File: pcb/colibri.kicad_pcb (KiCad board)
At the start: 2 copper layers, 55 parts

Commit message: diodes on place
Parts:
- ld-1, ld-10, ld-11, ld-12, ld-13, ld-14, ld-15, ld-16, ld-17, ld-18, ld-19, ld-2, ld-20, ld-21, ld-22, ld-23, ld-24, ld-25, ld-26, ld-27, ld-3, ld-4, ld-5, ld-6, ld-7, ld-8, ld-9: footprint kbd:D3_TH_SMD_v2 -> kbd:D3_SMD_v2; moved to B.Cu
- pro-micro1: moved to B.Cu
- moved ld-5 124.9 mm to (201.1, 52.0), turned to 90 degrees
- moved ld-10 114.8 mm to (182.0, 71.1), turned to 90 degrees
- moved ld-13 112.8 mm to (122.6, 90.1), turned to 90 degrees
- moved ld-3 111.8 mm to (163.0, 52.0), turned to 90 degrees
- moved ld-12 107.1 mm to (220.1, 71.1), turned to 90 degrees
- moved ld-27 104.9 mm to (222.1, 128.2), turned to 90 degrees
- moved ld-1 100.9 mm to (122.6, 52.0), turned to 90 degrees
- moved ld-23 92.9 mm to (201.1, 109.2), turned to 90 degrees
- moved ld-6 90.7 mm to (220.1, 52.0), turned to 90 degrees
- moved ld-8 90.4 mm to (143.9, 71.1), turned to 90 degrees
- moved ld-11 88.3 mm to (201.1, 71.1), turned to 90 degrees
- moved ld-7 84.3 mm to (122.6, 71.1), turned to 90 degrees
- moved ld-17 82.8 mm to (201.1, 90.1), turned to 90 degrees
- moved ld-26 77.7 mm to (194.1, 128.2), turned to 90 degrees
- moved ld-21 77.2 mm to (163.0, 109.2), turned to 90 degrees
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
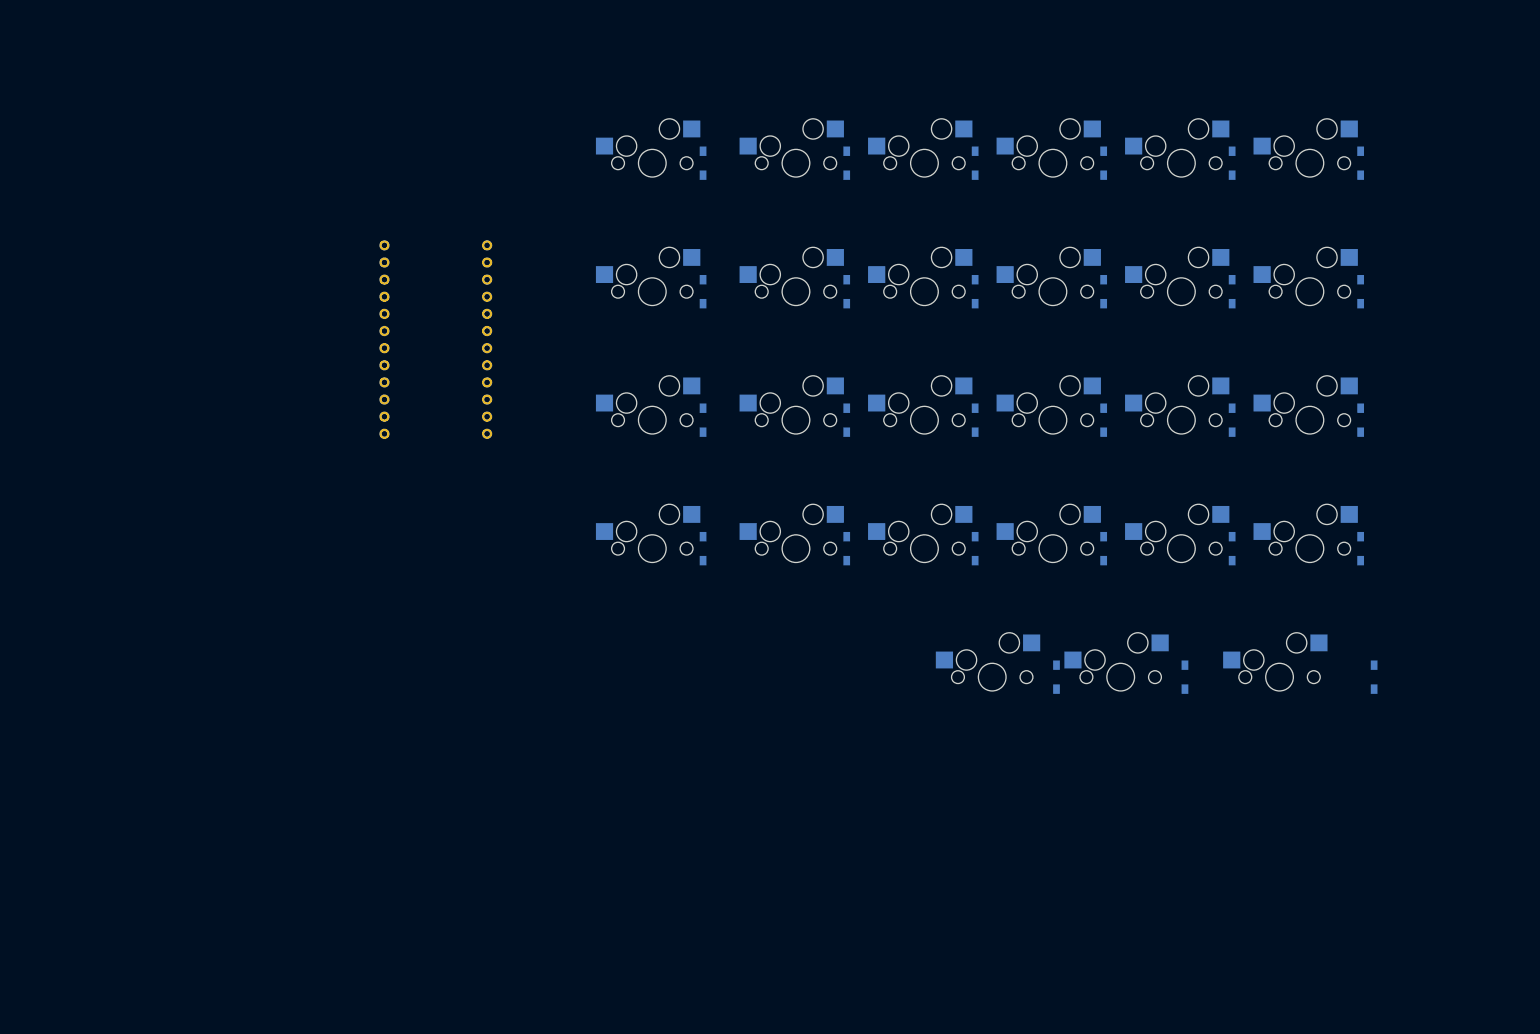
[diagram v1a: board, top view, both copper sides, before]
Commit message: LEDs placed on the PCB
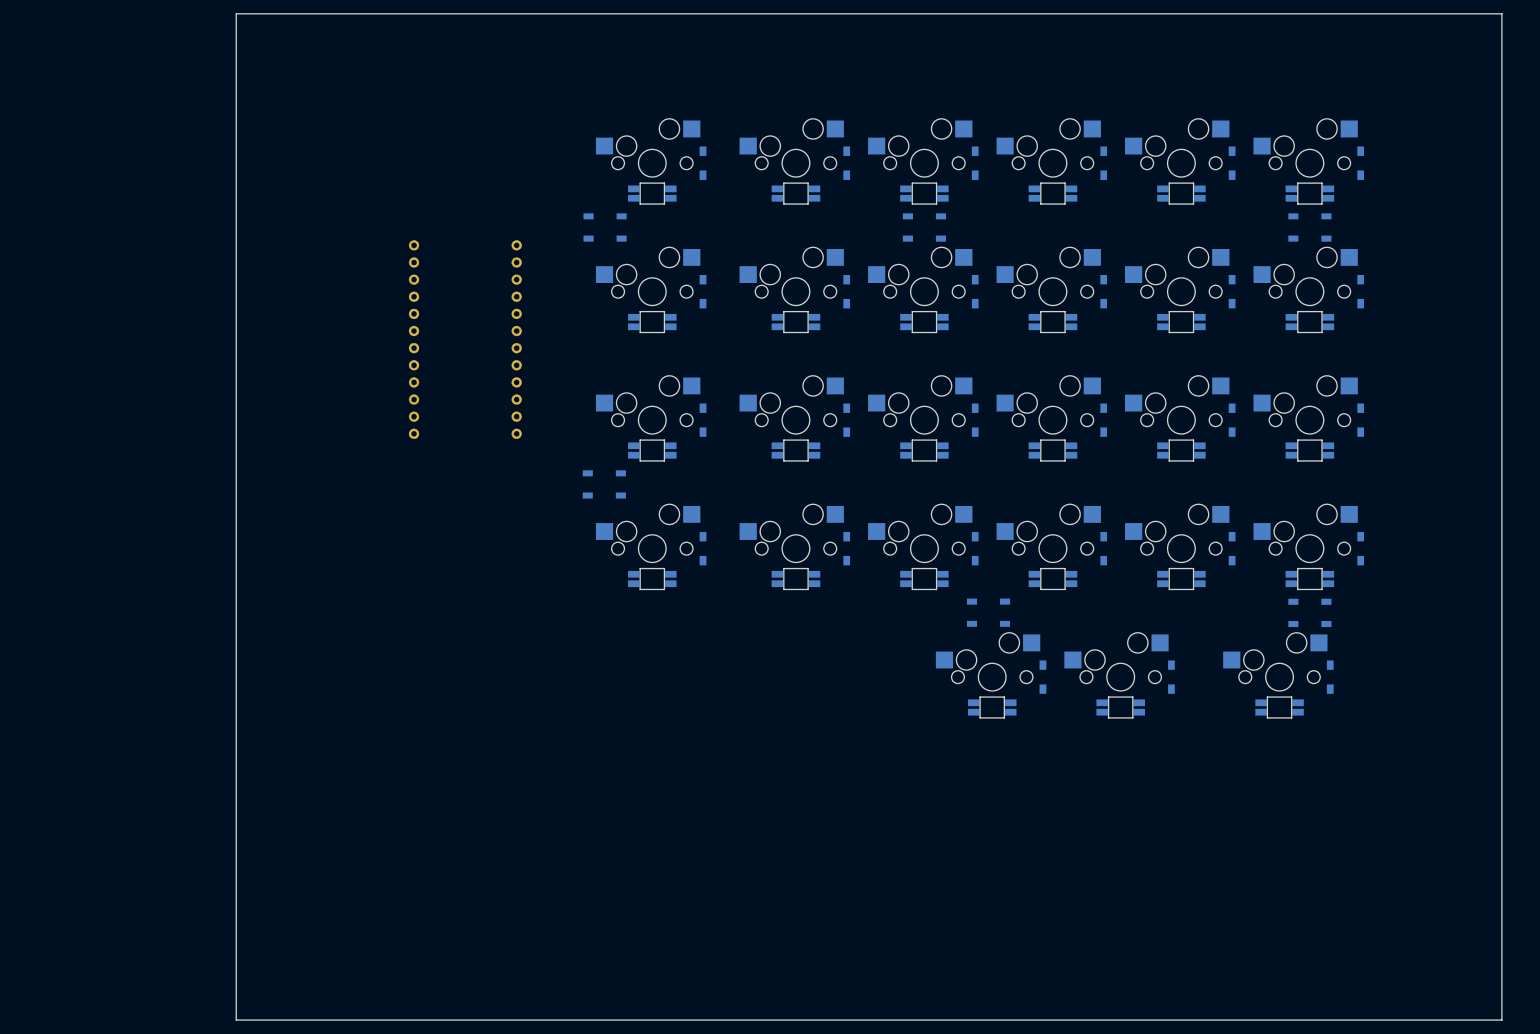
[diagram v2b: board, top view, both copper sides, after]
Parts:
- added lled-1: YS-SK6812MINI-E, kbd:YS-SK6812MINI-E, B.Cu at (115.1, 56.5)
- added lled-10: YS-SK6812MINI-E, kbd:YS-SK6812MINI-E, B.Cu at (174.5, 75.6)
- added lled-11: YS-SK6812MINI-E, kbd:YS-SK6812MINI-E, B.Cu at (193.6, 75.6)
- added lled-12: YS-SK6812MINI-E, kbd:YS-SK6812MINI-E, B.Cu at (212.6, 75.6)
- added lled-13: YS-SK6812MINI-E, kbd:YS-SK6812MINI-E, B.Cu at (115.1, 94.6)
- added lled-14: YS-SK6812MINI-E, kbd:YS-SK6812MINI-E, B.Cu at (136.4, 94.6)
- added lled-15: YS-SK6812MINI-E, kbd:YS-SK6812MINI-E, B.Cu at (155.5, 94.6)
- added lled-16: YS-SK6812MINI-E, kbd:YS-SK6812MINI-E, B.Cu at (174.5, 94.6)
- added lled-17: YS-SK6812MINI-E, kbd:YS-SK6812MINI-E, B.Cu at (193.6, 94.6)
- added lled-18: YS-SK6812MINI-E, kbd:YS-SK6812MINI-E, B.Cu at (212.6, 94.6)
- added lled-19: YS-SK6812MINI-E, kbd:YS-SK6812MINI-E, B.Cu at (115.1, 113.7)
- added lled-2: YS-SK6812MINI-E, kbd:YS-SK6812MINI-E, B.Cu at (136.4, 56.5)
- added lled-20: YS-SK6812MINI-E, kbd:YS-SK6812MINI-E, B.Cu at (136.4, 113.7)
- added lled-21: YS-SK6812MINI-E, kbd:YS-SK6812MINI-E, B.Cu at (155.5, 113.7)
- added lled-22: YS-SK6812MINI-E, kbd:YS-SK6812MINI-E, B.Cu at (174.5, 113.7)
- added lled-23: YS-SK6812MINI-E, kbd:YS-SK6812MINI-E, B.Cu at (193.6, 113.7)
- added lled-24: YS-SK6812MINI-E, kbd:YS-SK6812MINI-E, B.Cu at (212.6, 113.7)
- added lled-25: YS-SK6812MINI-E, kbd:YS-SK6812MINI-E, B.Cu at (165.5, 132.7)
- added lled-26: YS-SK6812MINI-E, kbd:YS-SK6812MINI-E, B.Cu at (184.6, 132.7)
- added lled-27: YS-SK6812MINI-E, kbd:YS-SK6812MINI-E, B.Cu at (208.1, 132.7)
- added lled-3: YS-SK6812MINI-E, kbd:YS-SK6812MINI-E, B.Cu at (155.5, 56.5)
- added lled-4: YS-SK6812MINI-E, kbd:YS-SK6812MINI-E, B.Cu at (174.5, 56.5)
- added lled-5: YS-SK6812MINI-E, kbd:YS-SK6812MINI-E, B.Cu at (193.6, 56.5)
- added lled-6: YS-SK6812MINI-E, kbd:YS-SK6812MINI-E, B.Cu at (212.6, 56.5)
- added lled-7: YS-SK6812MINI-E, kbd:YS-SK6812MINI-E, B.Cu at (115.1, 75.6)
- added lled-8: YS-SK6812MINI-E, kbd:YS-SK6812MINI-E, B.Cu at (136.4, 75.6)
- added lled-9: YS-SK6812MINI-E, kbd:YS-SK6812MINI-E, B.Cu at (155.5, 75.6)
- added lu-1: WS2812B, LED_SMD:LED_WS2812B_PLCC4_5.0x5.0mm_P3.2mm, B.Cu at (108.1, 61.6)
- added lu-2: WS2812B, LED_SMD:LED_WS2812B_PLCC4_5.0x5.0mm_P3.2mm, B.Cu at (155.5, 61.6)
- added lu-3: WS2812B, LED_SMD:LED_WS2812B_PLCC4_5.0x5.0mm_P3.2mm, B.Cu at (212.6, 61.6)
- added lu-4: WS2812B, LED_SMD:LED_WS2812B_PLCC4_5.0x5.0mm_P3.2mm, B.Cu at (108.0, 99.7)
- added lu-5: WS2812B, LED_SMD:LED_WS2812B_PLCC4_5.0x5.0mm_P3.2mm, B.Cu at (165.0, 118.7)
- added lu-6: WS2812B, LED_SMD:LED_WS2812B_PLCC4_5.0x5.0mm_P3.2mm, B.Cu at (212.6, 118.7)
- moved ld-27 6.50 mm to (215.6, 128.2)
- moved pro-micro1 4.39 mm to (87.4, 78.7)
- moved ld-25 2.00 mm to (173.0, 128.2)
- moved ld-26 2.00 mm to (192.1, 128.2)
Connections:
- pro-micro1 pad 1: unconnected-(pro-micro1-Pad1) -> lled
- pro-micro1 pad 2: unconnected-(pro-micro1-Pad2) -> ldata
- pro-micro1 pad 21: unconnected-(pro-micro1-Pad21) -> lVCC
- pro-micro1 pad 22: unconnected-(pro-micro1-Pad22) -> lreset
- pro-micro1 pad 23: unconnected-(pro-micro1-Pad23) -> lGND
- pro-micro1 pad 3: unconnected-(pro-micro1-Pad3) -> lGND
- pro-micro1 pad 4: unconnected-(pro-micro1-Pad4) -> lGND
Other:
- board outline added: 187.7 x 149.2 mm

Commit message: better keyboard layout
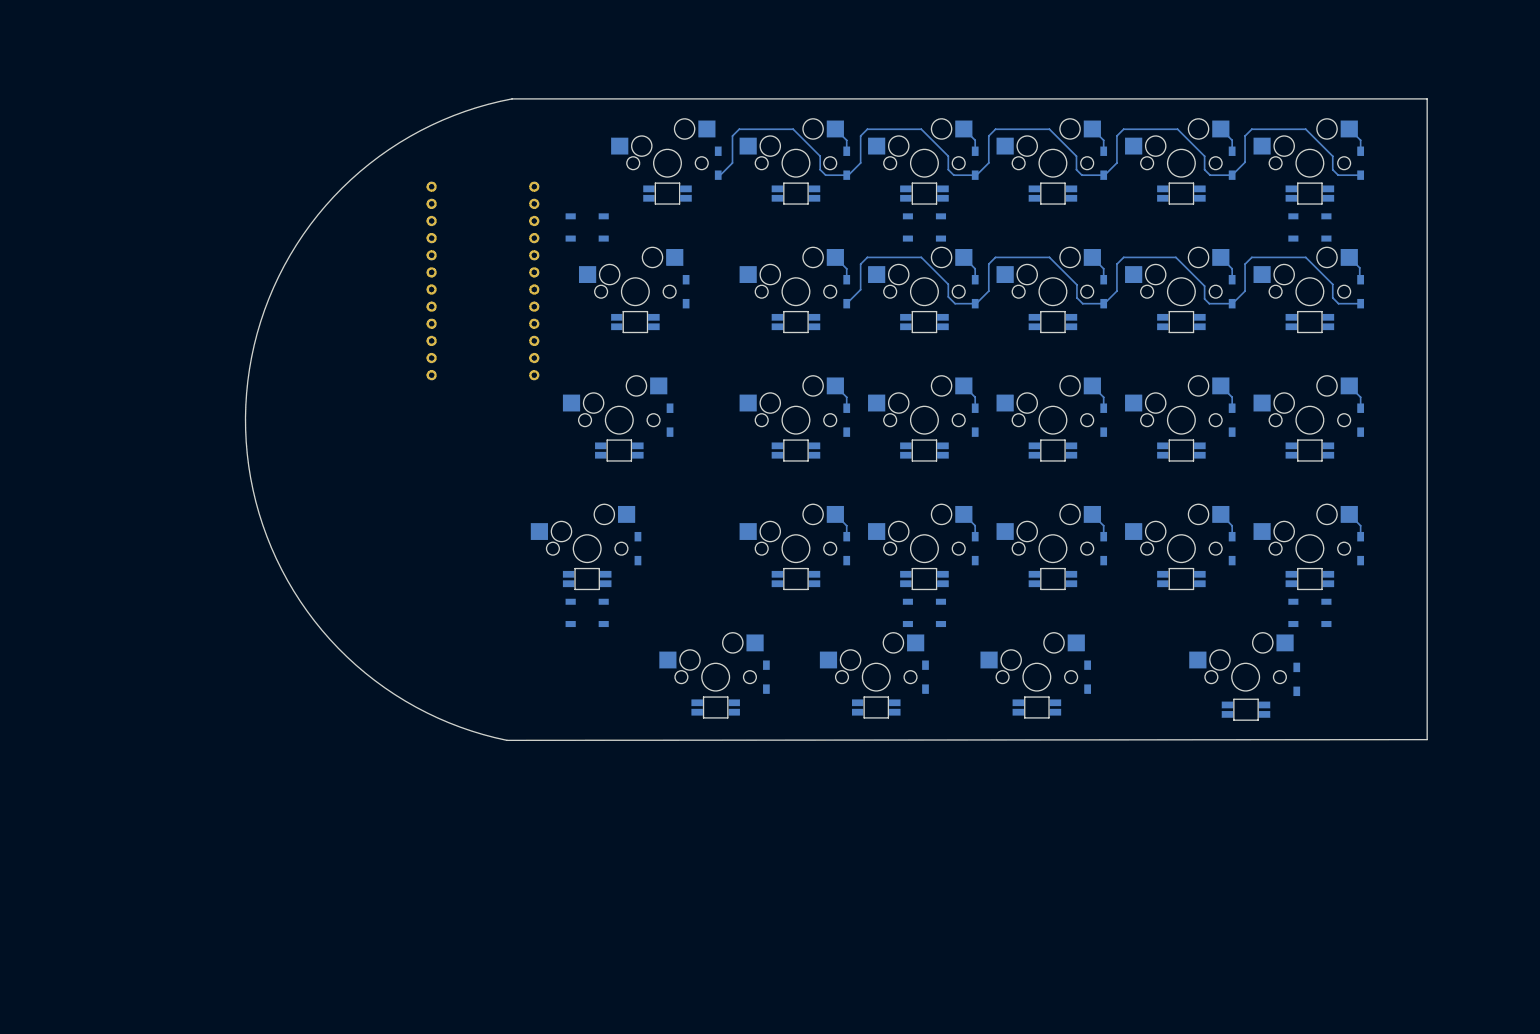
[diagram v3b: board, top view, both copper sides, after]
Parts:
- added ld-28: 1N4148W, kbd:D3_SMD_v2, B.Cu at (210.7, 128.6)
- added lled-28: YS-SK6812MINI-E, kbd:YS-SK6812MINI-E, B.Cu at (203.1, 133.1)
- added lsw-28: SW_PUSH, kbd:CherryMX_Hotswap_2u, F.Cu at (203.1, 128.2)
- lsw-1: footprint kbd:CherryMX_Hotswap_1.25U -> kbd:CherryMX_Hotswap
- lsw-13: footprint kbd:CherryMX_Hotswap_1.25U -> kbd:CherryMX_Hotswap_1.75u
- lsw-19: footprint kbd:CherryMX_Hotswap_1.25U -> kbd:CherryMX_Hotswap_2.25u
- lsw-25, lsw-26: footprint kbd:CherryMX_Hotswap -> kbd:CherryMX_Hotswap_1.25u
- lsw-27: footprint kbd:CherryMX_Hotswap_1.5u -> kbd:CherryMX_Hotswap_1.25u
- lsw-7: footprint kbd:CherryMX_Hotswap_1.25U -> kbd:CherryMX_Hotswap_1.5u
- moved ld-25 41.0 mm to (132.0, 128.2)
- moved lled-25 41.0 mm to (124.5, 132.7)
- moved lsw-25 41.0 mm to (124.5, 128.2)
- moved ld-26 36.5 mm to (155.6, 128.2)
- moved lled-26 36.2 mm to (148.3, 132.7)
- moved lsw-26 36.2 mm to (148.3, 128.2)
- moved ld-27 36.0 mm to (179.7, 128.2)
- moved lled-27 36.0 mm to (172.1, 132.7)
- moved lsw-27 36.0 mm to (172.1, 128.2)
- moved lu-4 19.2 mm to (105.5, 118.7)
- moved ld-19 9.66 mm to (113.0, 109.2)
- moved lled-19 9.66 mm to (105.5, 113.7)
- moved lsw-19 9.66 mm to (105.5, 109.2)
- moved lu-5 9.50 mm to (155.5, 118.7)
- moved pro-micro1 9.08 mm to (90.0, 70.0)
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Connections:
- lled-21 pad 4: Net-(lled-20-Pad2) -> Net-(lled-21-Pad4)
- lled-23 pad 4: Net-(lled-26-Pad2) -> Net-(lled-23-Pad4)
- lled-25 pad 1: Net-(lled-25-Pad1) -> unconnected-(lled-25-Pad1)
- lled-25 pad 2: Net-(lled-25-Pad2) -> Net-(lled-21-Pad4)
- lled-25 pad 4: Net-(lled-22-Pad2) -> Net-(lled-20-Pad2)
- lled-26 pad 1: Net-(lled-25-Pad1) -> Net-(lled-26-Pad1)
- lled-26 pad 3: lGND -> unconnected-(lled-26-Pad3)
- lled-26 pad 4: Net-(lled-25-Pad2) -> Net-(lled-22-Pad2)
- lled-27 pad 1: lVCC -> Net-(lled-26-Pad1)
- lled-27 pad 2: unconnected-(lled-27-Pad2) -> Net-(lled-23-Pad4)
- lled-27 pad 4: Net-(lled-24-Pad2) -> Net-(lled-26-Pad2)
- lsw-25 pad 1: lcol3 -> lcol2
- lsw-26 pad 1: lcol4 -> lcol3
- lsw-27 pad 1: lcol5 -> lcol4
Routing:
- net lrow0: track 0.00 -> 140.0 mm
- net lrow1: track 0.00 -> 112.4 mm
- net Net-(ld-20-Pad2): track 0.00 -> 4.00 mm
- net Net-(ld-2-Pad2): track 0.00 -> 4.00 mm
- net Net-(ld-8-Pad2): track 0.00 -> 4.00 mm
- net Net-(ld-14-Pad2): track 0.00 -> 4.00 mm
- net Net-(ld-24-Pad2): track 0.00 -> 4.00 mm
- net Net-(ld-23-Pad2): track 0.00 -> 4.00 mm
- net Net-(ld-22-Pad2): track 0.00 -> 4.00 mm
- net Net-(ld-21-Pad2): track 0.00 -> 4.00 mm
- net Net-(ld-6-Pad2): track 0.00 -> 4.00 mm
- net Net-(ld-5-Pad2): track 0.00 -> 4.00 mm
- net Net-(ld-4-Pad2): track 0.00 -> 4.00 mm
- net Net-(ld-3-Pad2): track 0.00 -> 4.00 mm
- net Net-(ld-9-Pad2): track 0.00 -> 4.00 mm
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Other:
- board size 187.7 x 149.2 mm -> 175.2 x 95.1 mm

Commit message: board size
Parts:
- moved pro-micro1 53.3 mm to (37.4, 61.1)
- moved ld-10 48.6 mm to (133.5, 68.5)
- moved ld-12 48.6 mm to (171.6, 68.5)
- moved ld-14 48.6 mm to (95.4, 87.5)
- moved ld-16 48.6 mm to (133.5, 87.5)
- moved ld-18 48.6 mm to (171.6, 87.5)
- moved ld-19 48.6 mm to (64.4, 106.5)
- moved ld-2 48.6 mm to (95.4, 49.4)
- moved ld-20 48.6 mm to (95.4, 106.5)
- moved ld-22 48.6 mm to (133.5, 106.5)
- moved ld-24 48.6 mm to (171.6, 106.5)
- moved ld-25 48.6 mm to (83.5, 125.6)
- moved ld-27 48.6 mm to (131.1, 125.6)
- moved ld-4 48.6 mm to (133.5, 49.4)
- moved ld-6 48.6 mm to (171.6, 49.4)
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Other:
- board size 175.2 x 95.1 mm -> 160 x 94.7 mm

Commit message: rows connected
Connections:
- lsw-25 pad 1: lcol2 -> lcol1
- lsw-26 pad 1: lcol3 -> lcol2
- lsw-27 pad 1: lcol4 -> lcol3
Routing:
- net lrow3: track 0.00 -> 151.7 mm
- net lrow2: track 0.00 -> 146.7 mm
- net lrow4: track 0.00 -> 105.5 mm
- net lrow1: track 112.4 -> 144.4 mm
- net Net-(ld-28-Pad2): track 0.00 -> 4.35 mm
- net Net-(ld-27-Pad2): track 0.00 -> 4.00 mm
- net Net-(ld-25-Pad2): track 0.00 -> 4.00 mm
- net Net-(ld-26-Pad2): track 0.00 -> 3.91 mm
- net lrow0: track 140.0 -> 139.0 mm

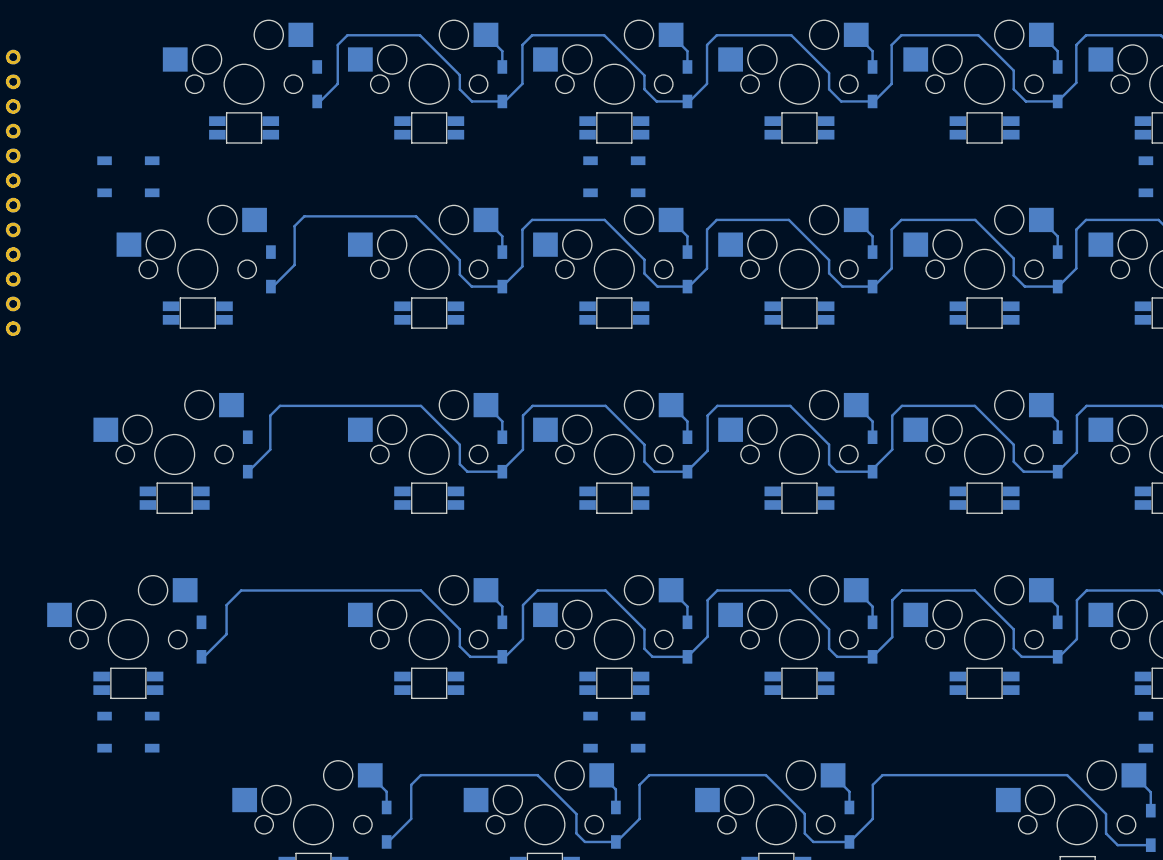
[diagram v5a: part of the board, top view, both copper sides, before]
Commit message: columns connected
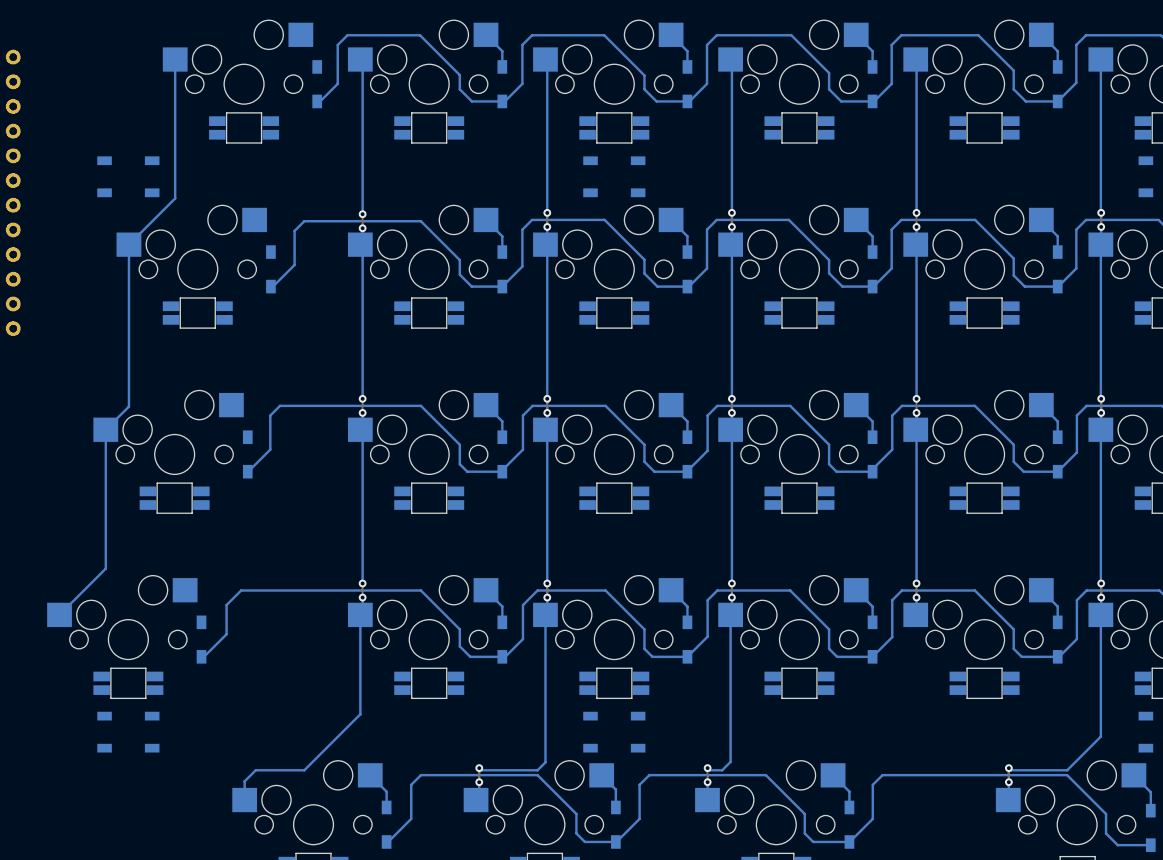
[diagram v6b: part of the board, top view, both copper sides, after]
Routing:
- net lcol1: track 0.00 -> 84.6 mm, vias 0 -> 6
- net lcol5: track 0.00 -> 84.1 mm, vias 0 -> 8
- net lcol2: track 0.00 -> 83.5 mm, vias 0 -> 8
- net lcol3: track 0.00 -> 78.7 mm, vias 0 -> 8
- net lcol0: track 0.00 -> 62.1 mm
- net lcol4: track 0.00 -> 57.4 mm, vias 0 -> 6
- net lrow1: track 144.4 -> 143.7 mm
